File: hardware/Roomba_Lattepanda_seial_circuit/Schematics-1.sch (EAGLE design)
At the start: 5 parts

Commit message: local server
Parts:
- removed D1: U57X32, led:U57X32
- removed JP10, JP6: (no value), adafruit:PINHD-1X1
- added JP1, JP2, JP3, JP4, JP5: (no value), adafruit:PINHD-1X1CB
- added LD2: (no value), led:DUOLED-RY-C
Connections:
- new net N$2: JP1.1, JP4.1
- new net N$5: JP5.1, LD2.AY
- new net N$7: JP2.1, LD2.C
- net N$4: now also JP3.1, LD2.AR; no longer D1.A
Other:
- note added: "GND"
- note added: "PWR"
- note added: "Pin 10"
- note added: "Pin 5"
- note added: "pin 11"
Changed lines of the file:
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@@
 </classes>
 <parts>
-<part name="JP6" library="adafruit" deviceset="PINHD-1X1" device=""/>
-<part name="JP10" library="adafruit" deviceset="PINHD-1X1" device=""/>
 <part name="LD1" library="led" deviceset="DUOLED-RY-C" device=""/>
-<part name="D1" library="led" deviceset="U57X32" device=""/>
 <part name="D2" library="led" deviceset="U57X32" device=""/>
+<part name="JP1" library="adafruit" deviceset="PINHD-1X1" device="CB"/>
+<part name="LD2" library="led" deviceset="DUOLED-RY-C" device=""/>
+<part name="JP2" library="adafruit" deviceset="PINHD-1X1" device="CB"/>
+<part name="JP4" library="adafruit" deviceset="PINHD-1X1" device="CB"/>
+<part name="JP3" library="adafruit" deviceset="PINHD-1X1" device="CB"/>
+<part name="JP5" library="adafruit" deviceset="PINHD-1X1" device="CB"/>
 </parts>
 <sheets>
 <sheet>
 <plain>
+<text x="0" y="60.96" size="1.778" layer="91">Pin 10</text>
+<text x="0" y="50.8" size="1.778" layer="91">pin 11</text>
+<text x="0" y="30.48" size="1.778" layer="91">GND</text>
+<text x="0" y="15.24" size="1.778" layer="91">Pin 5</text>
+<text x="0" y="2.54" size="1.778" layer="91">PWR</text>
+<text x="-15.24" y="48.26" size="1.778" layer="91">PWR</text>
 </plain>
 <instances>
-<instance part="JP6" gate="G$1" x="27.94" y="58.42"/>
-<instance part="JP10" gate="G$1" x="27.94" y="30.48"/>
 <instance part="LD1" gate="G$1" x="40.64" y="45.72"/>
-<instance part="D1" gate="1" x="10.16" y="33.02"/>
 <instance part="D2" gate="1" x="10.16" y="58.42"/>
+<instance part="JP1" gate="G$1" x="17.78" y="15.24"/>
+<instance part="LD2" gate="G$1" x="40.64" y="15.24"/>
+<instance part="JP2" gate="G$1" x="30.48" y="15.24" rot="R180"/>
+<instance part="JP4" gate="G$1" x="25.4" y="15.24"/>
+<instance part="JP3" gate="G$1" x="7.62" y="35.56" rot="R180"/>
+<instance part="JP5" gate="G$1" x="7.62" y="27.94" rot="R180"/>
 </instances>
 <busses>
@@
 <segment>
 <wire x1="10.16" y1="35.56" x2="10.16" y2="40.64" width="0.1524" layer="91"/>
-<pinref part="D1" gate="1" pin="A"/>
 <wire x1="10.16" y1="40.64" x2="35.56" y2="40.64" width="0.1524" layer="91"/>
 <wire x1="35.56" y1="40.64" x2="35.56" y2="38.1" width="0.1524" layer="91"/>
 <pinref part="LD1" gate="G$1" pin="AY"/>
+<pinref part="LD2" gate="G$1" pin="AR"/>
 <wire x1="35.56" y1="38.1" x2="40.64" y2="38.1" width="0.1524" layer="91"/>
+<wire x1="40.64" y1="38.1" x2="40.64" y2="22.86" width="0.1524" layer="91"/>
+<pinref part="JP3" gate="G$1" pin="1"/>
 </segment>
 </net>
@@
 </segment>
 </net>
+<net name="N$2" class="0">
+<segment>
+<wire x1="15.24" y1="15.24" x2="22.86" y2="15.24" width="0.1524" layer="91"/>
+<pinref part="JP1" gate="G$1" pin="1"/>
+<pinref part="JP4" gate="G$1" pin="1"/>
+</segment>
+</net>
+<net name="N$5" class="0">
+<segment>
+<pinref part="LD2" gate="G$1" pin="AY"/>
+<wire x1="40.64" y1="2.54" x2="40.64" y2="7.62" width="0.1524" layer="91"/>
+<wire x1="10.16" y1="27.94" x2="10.16" y2="2.54" width="0.1524" layer="91"/>
+<wire x1="10.16" y1="2.54" x2="40.64" y2="2.54" width="0.1524" layer="91"/>
+<pinref part="JP5" gate="G$1" pin="1"/>
+</segment>
+</net>
+<net name="N$7" class="0">
+<segment>
+<pinref part="LD2" gate="G$1" pin="C"/>
+<pinref part="JP2" gate="G$1" pin="1"/>
+<wire x1="33.02" y1="15.24" x2="38.1" y2="15.24" width="0.1524" layer="91"/>
+</segment>
+</net>

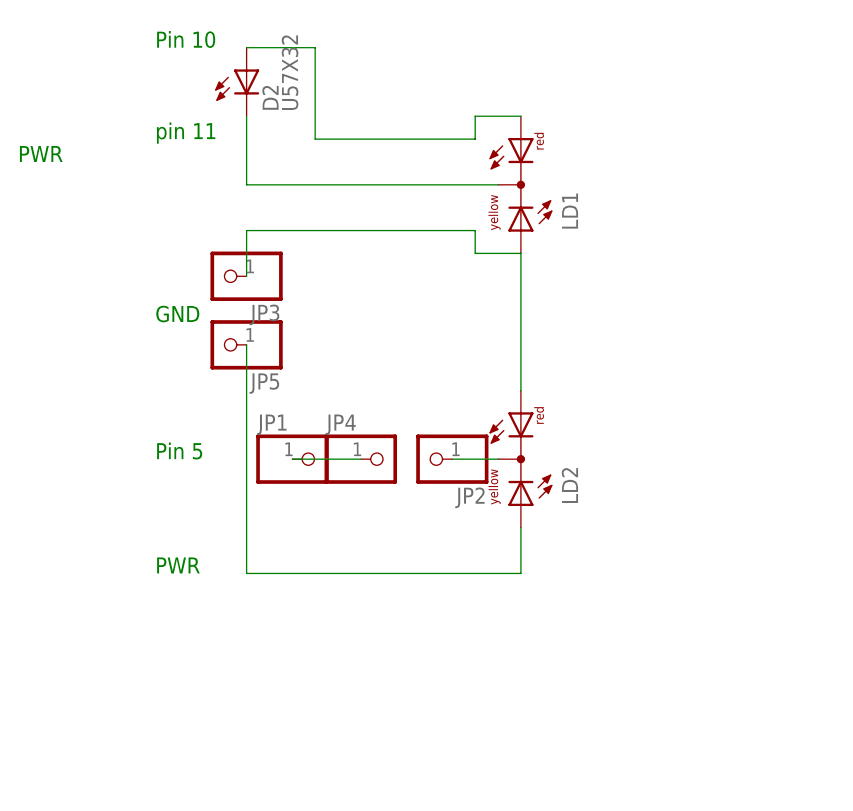
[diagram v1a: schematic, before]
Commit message: add new board/ add perfect stitch helper
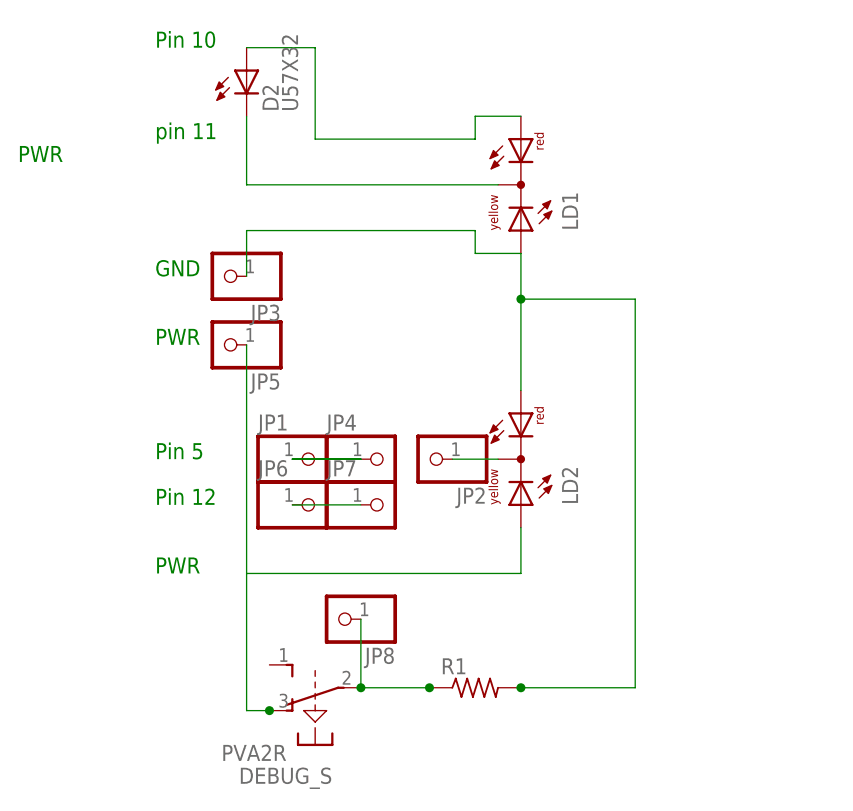
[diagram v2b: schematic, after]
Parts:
- added DEBUG_S: PVA2R, switch-misc:PVA2R
- added JP6, JP7, JP8: (no value), adafruit:PINHD-1X1CB
- added R1: (no value), adafruit:R-US_0204/7
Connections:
- new net N$6: DEBUG_S1.P, JP8.1, R1.1
- new net N$8: JP6.1, JP7.1
- net N$4: now also R1.2
- net N$5: now also DEBUG_S1.O
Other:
- note added: "Pin 12"
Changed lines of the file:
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@@
 <part name="JP3" library="adafruit" deviceset="PINHD-1X1" device="CB"/>
 <part name="JP5" library="adafruit" deviceset="PINHD-1X1" device="CB"/>
+<part name="R1" library="adafruit" deviceset="R-US_" device="0204/7"/>
+<part name="DEBUG_S" library="switch-misc" deviceset="PVA2R" device=""/>
+<part name="JP6" library="adafruit" deviceset="PINHD-1X1" device="CB"/>
+<part name="JP7" library="adafruit" deviceset="PINHD-1X1" device="CB"/>
+<part name="JP8" library="adafruit" deviceset="PINHD-1X1" device="CB"/>
 </parts>
 <sheets>
@@
 <text x="0" y="60.96" size="1.778" layer="91">Pin 10</text>
 <text x="0" y="50.8" size="1.778" layer="91">pin 11</text>
-<text x="0" y="30.48" size="1.778" layer="91">GND</text>
 <text x="0" y="15.24" size="1.778" layer="91">Pin 5</text>
 <text x="0" y="2.54" size="1.778" layer="91">PWR</text>
 <text x="-15.24" y="48.26" size="1.778" layer="91">PWR</text>
+<text x="0" y="27.94" size="1.778" layer="91">PWR</text>
+<text x="0" y="35.56" size="1.778" layer="91">GND</text>
+<text x="0" y="10.16" size="1.778" layer="91">Pin 12</text>
 </plain>
 <instances>
@@
 <instance part="JP3" gate="G$1" x="7.62" y="35.56" rot="R180"/>
 <instance part="JP5" gate="G$1" x="7.62" y="27.94" rot="R180"/>
+<instance part="R1" gate="G$1" x="35.56" y="-10.16"/>
+<instance part="DEBUG_S" gate="1" x="17.78" y="-10.16" rot="R90"/>
+<instance part="JP6" gate="G$1" x="17.78" y="10.16"/>
+<instance part="JP7" gate="G$1" x="25.4" y="10.16"/>
+<instance part="JP8" gate="G$1" x="20.32" y="-2.54" rot="R180"/>
 </instances>
 <busses>
@@
 <pinref part="LD2" gate="G$1" pin="AR"/>
 <wire x1="35.56" y1="38.1" x2="40.64" y2="38.1" width="0.1524" layer="91"/>
-<wire x1="40.64" y1="38.1" x2="40.64" y2="22.86" width="0.1524" layer="91"/>
+<wire x1="40.64" y1="38.1" x2="40.64" y2="33.02" width="0.1524" layer="91"/>
 <pinref part="JP3" gate="G$1" pin="1"/>
+<pinref part="R1" gate="G$1" pin="2"/>
+<wire x1="40.64" y1="33.02" x2="40.64" y2="22.86" width="0.1524" layer="91"/>
+<wire x1="40.64" y1="-10.16" x2="53.34" y2="-10.16" width="0.1524" layer="91"/>
+<wire x1="53.34" y1="-10.16" x2="53.34" y2="33.02" width="0.1524" layer="91"/>
+<wire x1="53.34" y1="33.02" x2="40.64" y2="33.02" width="0.1524" layer="91"/>
+<junction x="40.64" y="33.02"/>
+<junction x="40.64" y="-10.16"/>
 </segment>
 </net>
@@
 <pinref part="JP1" gate="G$1" pin="1"/>
 <pinref part="JP4" gate="G$1" pin="1"/>
+<wire x1="15.24" y1="15.24" x2="22.86" y2="15.24" width="0.1524" layer="91"/>
+<wire x1="15.24" y1="15.24" x2="22.86" y2="15.24" width="0.1524" layer="91"/>
 </segment>
 </net>
@@
 <wire x1="10.16" y1="2.54" x2="40.64" y2="2.54" width="0.1524" layer="91"/>
 <pinref part="JP5" gate="G$1" pin="1"/>
+<wire x1="10.16" y1="2.54" x2="10.16" y2="-12.7" width="0.1524" layer="91"/>
+<pinref part="DEBUG_S" gate="1" pin="O"/>
+<wire x1="10.16" y1="-12.7" x2="12.7" y2="-12.7" width="0.1524" layer="91"/>
+<junction x="12.7" y="-12.7"/>
 </segment>
 </net>
@@
 </segment>
 </net>
+<net name="N$6" class="0">
+<segment>
+<pinref part="R1" gate="G$1" pin="1"/>
+<wire x1="22.86" y1="-10.16" x2="30.48" y2="-10.16" width="0.1524" layer="91"/>
+<pinref part="DEBUG_S" gate="1" pin="P"/>
+<junction x="22.86" y="-10.16"/>
+<junction x="30.48" y="-10.16"/>
+<pinref part="JP8" gate="G$1" pin="1"/>
+<wire x1="22.86" y1="-2.54" x2="22.86" y2="-10.16" width="0.1524" layer="91"/>
+</segment>
+</net>
+<net name="N$8" class="0">
+<segment>
+<pinref part="JP6" gate="G$1" pin="1"/>
+<pinref part="JP7" gate="G$1" pin="1"/>
+<wire x1="15.24" y1="10.16" x2="22.86" y2="10.16" width="0.1524" layer="91"/>
+</segment>
+</net>

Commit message: add new concept art to repo + fix the style of media list + toggle augment
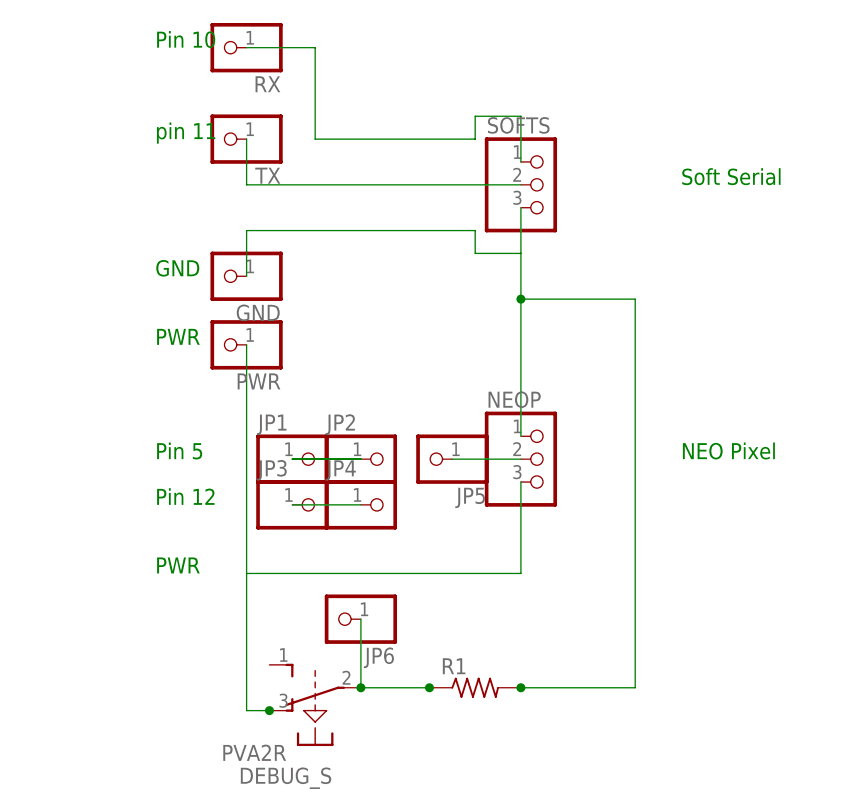
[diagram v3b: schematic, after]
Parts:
- removed D2: U57X32, led:U57X32
- removed JP7, JP8: (no value), adafruit:PINHD-1X1CB
- removed LD1, LD2: (no value), led:DUOLED-RY-C
- added GND, PWR, RX, TX: (no value), adafruit:PINHD-1X1CB
- added NEOP, SOFTS: (no value), adafruit:PINHD-1X3CB
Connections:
- net N$1: now also RX.1, SOFTS.1; no longer D2.A, LD1.AR
- net N$2: now also JP2.1; no longer JP4.1
- net N$3: now also SOFTS.2, TX.1; no longer D2.C, LD1.C
- net N$4: now also GND.1, NEOP.1, SOFTS.3; no longer JP3.1, LD1.AY, LD2.AR
- net N$5: now also NEOP.3, PWR.1; no longer JP5.1, LD2.AY
- net N$6: now also JP6.1; no longer JP8.1
- net N$7: now also JP5.1, NEOP.2; no longer JP2.1, LD2.C
- net N$8: now also JP3.1, JP4.1; no longer JP6.1, JP7.1
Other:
- note added: "NEO Pixel"
- note added: "Soft Serial"
- moved on the sheet: JP2, JP3, JP4, JP5, JP6
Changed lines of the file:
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@@
 </classes>
 <parts>
-<part name="LD1" library="led" deviceset="DUOLED-RY-C" device=""/>
-<part name="D2" library="led" deviceset="U57X32" device=""/>
 <part name="JP1" library="adafruit" deviceset="PINHD-1X1" device="CB"/>
-<part name="LD2" library="led" deviceset="DUOLED-RY-C" device=""/>
+<part name="JP5" library="adafruit" deviceset="PINHD-1X1" device="CB"/>
 <part name="JP2" library="adafruit" deviceset="PINHD-1X1" device="CB"/>
-<part name="JP4" library="adafruit" deviceset="PINHD-1X1" device="CB"/>
-<part name="JP3" library="adafruit" deviceset="PINHD-1X1" device="CB"/>
-<part name="JP5" library="adafruit" deviceset="PINHD-1X1" device="CB"/>
+<part name="GND" library="adafruit" deviceset="PINHD-1X1" device="CB"/>
+<part name="PWR" library="adafruit" deviceset="PINHD-1X1" device="CB"/>
 <part name="R1" library="adafruit" deviceset="R-US_" device="0204/7"/>
 <part name="DEBUG_S" library="switch-misc" deviceset="PVA2R" device=""/>
+<part name="JP3" library="adafruit" deviceset="PINHD-1X1" device="CB"/>
+<part name="JP4" library="adafruit" deviceset="PINHD-1X1" device="CB"/>
 <part name="JP6" library="adafruit" deviceset="PINHD-1X1" device="CB"/>
-<part name="JP7" library="adafruit" deviceset="PINHD-1X1" device="CB"/>
-<part name="JP8" library="adafruit" deviceset="PINHD-1X1" device="CB"/>
+<part name="NEOP" library="adafruit" deviceset="PINHD-1X3" device="CB"/>
+<part name="SOFTS" library="adafruit" deviceset="PINHD-1X3" device="CB"/>
+<part name="RX" library="adafruit" deviceset="PINHD-1X1" device="CB"/>
+<part name="TX" library="adafruit" deviceset="PINHD-1X1" device="CB"/>
 </parts>
 <sheets>
@@
 <text x="0" y="15.24" size="1.778" layer="91">Pin 5</text>
 <text x="0" y="2.54" size="1.778" layer="91">PWR</text>
-<text x="-15.24" y="48.26" size="1.778" layer="91">PWR</text>
 <text x="0" y="27.94" size="1.778" layer="91">PWR</text>
 <text x="0" y="35.56" size="1.778" layer="91">GND</text>
 <text x="0" y="10.16" size="1.778" layer="91">Pin 12</text>
+<text x="58.42" y="45.72" size="1.778" layer="91">Soft Serial</text>
+<text x="58.42" y="15.24" size="1.778" layer="91">NEO Pixel</text>
 </plain>
 <instances>
-<instance part="LD1" gate="G$1" x="40.64" y="45.72"/>
-<instance part="D2" gate="1" x="10.16" y="58.42"/>
 <instance part="JP1" gate="G$1" x="17.78" y="15.24"/>
-<instance part="LD2" gate="G$1" x="40.64" y="15.24"/>
-<instance part="JP2" gate="G$1" x="30.48" y="15.24" rot="R180"/>
-<instance part="JP4" gate="G$1" x="25.4" y="15.24"/>
-<instance part="JP3" gate="G$1" x="7.62" y="35.56" rot="R180"/>
-<instance part="JP5" gate="G$1" x="7.62" y="27.94" rot="R180"/>
+<instance part="JP5" gate="G$1" x="30.48" y="15.24" rot="R180"/>
+<instance part="JP2" gate="G$1" x="25.4" y="15.24"/>
+<instance part="GND" gate="G$1" x="7.62" y="35.56" rot="R180"/>
+<instance part="PWR" gate="G$1" x="7.62" y="27.94" rot="R180"/>
 <instance part="R1" gate="G$1" x="35.56" y="-10.16"/>
 <instance part="DEBUG_S" gate="1" x="17.78" y="-10.16" rot="R90"/>
-<instance part="JP6" gate="G$1" x="17.78" y="10.16"/>
-<instance part="JP7" gate="G$1" x="25.4" y="10.16"/>
-<instance part="JP8" gate="G$1" x="20.32" y="-2.54" rot="R180"/>
+<instance part="JP3" gate="G$1" x="17.78" y="10.16"/>
+<instance part="JP4" gate="G$1" x="25.4" y="10.16"/>
+<instance part="JP6" gate="G$1" x="20.32" y="-2.54" rot="R180"/>
+<instance part="NEOP" gate="A" x="43.18" y="15.24"/>
+<instance part="SOFTS" gate="A" x="43.18" y="45.72"/>
+<instance part="RX" gate="G$1" x="7.62" y="60.96" rot="R180"/>
+<instance part="TX" gate="G$1" x="7.62" y="50.8" rot="R180"/>
 </instances>
 <busses>
@@
 <segment>
 <wire x1="17.78" y1="60.96" x2="17.78" y2="50.8" width="0.1524" layer="91"/>
-<pinref part="D2" gate="1" pin="A"/>
-<wire x1="10.16" y1="60.96" x2="17.78" y2="60.96" width="0.1524" layer="91"/>
 <wire x1="17.78" y1="50.8" x2="35.56" y2="50.8" width="0.1524" layer="91"/>
 <wire x1="35.56" y1="50.8" x2="35.56" y2="53.34" width="0.1524" layer="91"/>
-<pinref part="LD1" gate="G$1" pin="AR"/>
 <wire x1="35.56" y1="53.34" x2="40.64" y2="53.34" width="0.1524" layer="91"/>
+<pinref part="SOFTS" gate="A" pin="1"/>
+<wire x1="40.64" y1="53.34" x2="40.64" y2="48.26" width="0.1524" layer="91"/>
+<pinref part="RX" gate="G$1" pin="1"/>
+<wire x1="17.78" y1="60.96" x2="10.16" y2="60.96" width="0.1524" layer="91"/>
 </segment>
 </net>
@@
 <wire x1="10.16" y1="40.64" x2="35.56" y2="40.64" width="0.1524" layer="91"/>
 <wire x1="35.56" y1="40.64" x2="35.56" y2="38.1" width="0.1524" layer="91"/>
-<pinref part="LD1" gate="G$1" pin="AY"/>
-<pinref part="LD2" gate="G$1" pin="AR"/>
 <wire x1="35.56" y1="38.1" x2="40.64" y2="38.1" width="0.1524" layer="91"/>
 <wire x1="40.64" y1="38.1" x2="40.64" y2="33.02" width="0.1524" layer="91"/>
-<pinref part="JP3" gate="G$1" pin="1"/>
+<pinref part="GND" gate="G$1" pin="1"/>
 <pinref part="R1" gate="G$1" pin="2"/>
-<wire x1="40.64" y1="33.02" x2="40.64" y2="22.86" width="0.1524" layer="91"/>
+<wire x1="40.64" y1="33.02" x2="40.64" y2="17.78" width="0.1524" layer="91"/>
 <wire x1="40.64" y1="-10.16" x2="53.34" y2="-10.16" width="0.1524" layer="91"/>
 <wire x1="53.34" y1="-10.16" x2="53.34" y2="33.02" width="0.1524" layer="91"/>
@@
 <junction x="40.64" y="33.02"/>
 <junction x="40.64" y="-10.16"/>
+<pinref part="SOFTS" gate="A" pin="3"/>
+<wire x1="40.64" y1="38.1" x2="40.64" y2="43.18" width="0.1524" layer="91"/>
+<pinref part="NEOP" gate="A" pin="1"/>
 </segment>
 </net>
 <net name="N$3" class="0">
 <segment>
-<pinref part="D2" gate="1" pin="C"/>
-<wire x1="10.16" y1="53.34" x2="10.16" y2="45.72" width="0.1524" layer="91"/>
-<pinref part="LD1" gate="G$1" pin="C"/>
-<wire x1="38.1" y1="45.72" x2="10.16" y2="45.72" width="0.1524" layer="91"/>
+<wire x1="40.64" y1="45.72" x2="10.16" y2="45.72" width="0.1524" layer="91"/>
+<pinref part="SOFTS" gate="A" pin="2"/>
+<wire x1="10.16" y1="45.72" x2="10.16" y2="50.8" width="0.1524" layer="91"/>
+<pinref part="TX" gate="G$1" pin="1"/>
 </segment>
 </net>
@@
 <wire x1="15.24" y1="15.24" x2="22.86" y2="15.24" width="0.1524" layer="91"/>
 <pinref part="JP1" gate="G$1" pin="1"/>
-<pinref part="JP4" gate="G$1" pin="1"/>
+<pinref part="JP2" gate="G$1" pin="1"/>
 <wire x1="15.24" y1="15.24" x2="22.86" y2="15.24" width="0.1524" layer="91"/>
 <wire x1="15.24" y1="15.24" x2="22.86" y2="15.24" width="0.1524" layer="91"/>
@@
 <net name="N$5" class="0">
 <segment>
-<pinref part="LD2" gate="G$1" pin="AY"/>
-<wire x1="40.64" y1="2.54" x2="40.64" y2="7.62" width="0.1524" layer="91"/>
 <wire x1="10.16" y1="27.94" x2="10.16" y2="2.54" width="0.1524" layer="91"/>
 <wire x1="10.16" y1="2.54" x2="40.64" y2="2.54" width="0.1524" layer="91"/>
-<pinref part="JP5" gate="G$1" pin="1"/>
+<pinref part="PWR" gate="G$1" pin="1"/>
 <wire x1="10.16" y1="2.54" x2="10.16" y2="-12.7" width="0.1524" layer="91"/>
 <pinref part="DEBUG_S" gate="1" pin="O"/>
 <wire x1="10.16" y1="-12.7" x2="12.7" y2="-12.7" width="0.1524" layer="91"/>
 <junction x="12.7" y="-12.7"/>
+<pinref part="NEOP" gate="A" pin="3"/>
+<wire x1="40.64" y1="2.54" x2="40.64" y2="12.7" width="0.1524" layer="91"/>
 </segment>
 </net>
 <net name="N$7" class="0">
 <segment>
-<pinref part="LD2" gate="G$1" pin="C"/>
-<pinref part="JP2" gate="G$1" pin="1"/>
-<wire x1="33.02" y1="15.24" x2="38.1" y2="15.24" width="0.1524" layer="91"/>
+<pinref part="JP5" gate="G$1" pin="1"/>
+<wire x1="33.02" y1="15.24" x2="40.64" y2="15.24" width="0.1524" layer="91"/>
+<pinref part="NEOP" gate="A" pin="2"/>
 </segment>
 </net>
@@
 <junction x="22.86" y="-10.16"/>
 <junction x="30.48" y="-10.16"/>
-<pinref part="JP8" gate="G$1" pin="1"/>
+<pinref part="JP6" gate="G$1" pin="1"/>
 <wire x1="22.86" y1="-2.54" x2="22.86" y2="-10.16" width="0.1524" layer="91"/>
 </segment>
@@
 <net name="N$8" class="0">
 <segment>
-<pinref part="JP6" gate="G$1" pin="1"/>
-<pinref part="JP7" gate="G$1" pin="1"/>
+<pinref part="JP3" gate="G$1" pin="1"/>
+<pinref part="JP4" gate="G$1" pin="1"/>
 <wire x1="15.24" y1="10.16" x2="22.86" y2="10.16" width="0.1524" layer="91"/>
 </segment>
